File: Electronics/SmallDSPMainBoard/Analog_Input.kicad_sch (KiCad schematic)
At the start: 57 parts, among them J11 NC3FAAH2, J12 NC3FAAH2

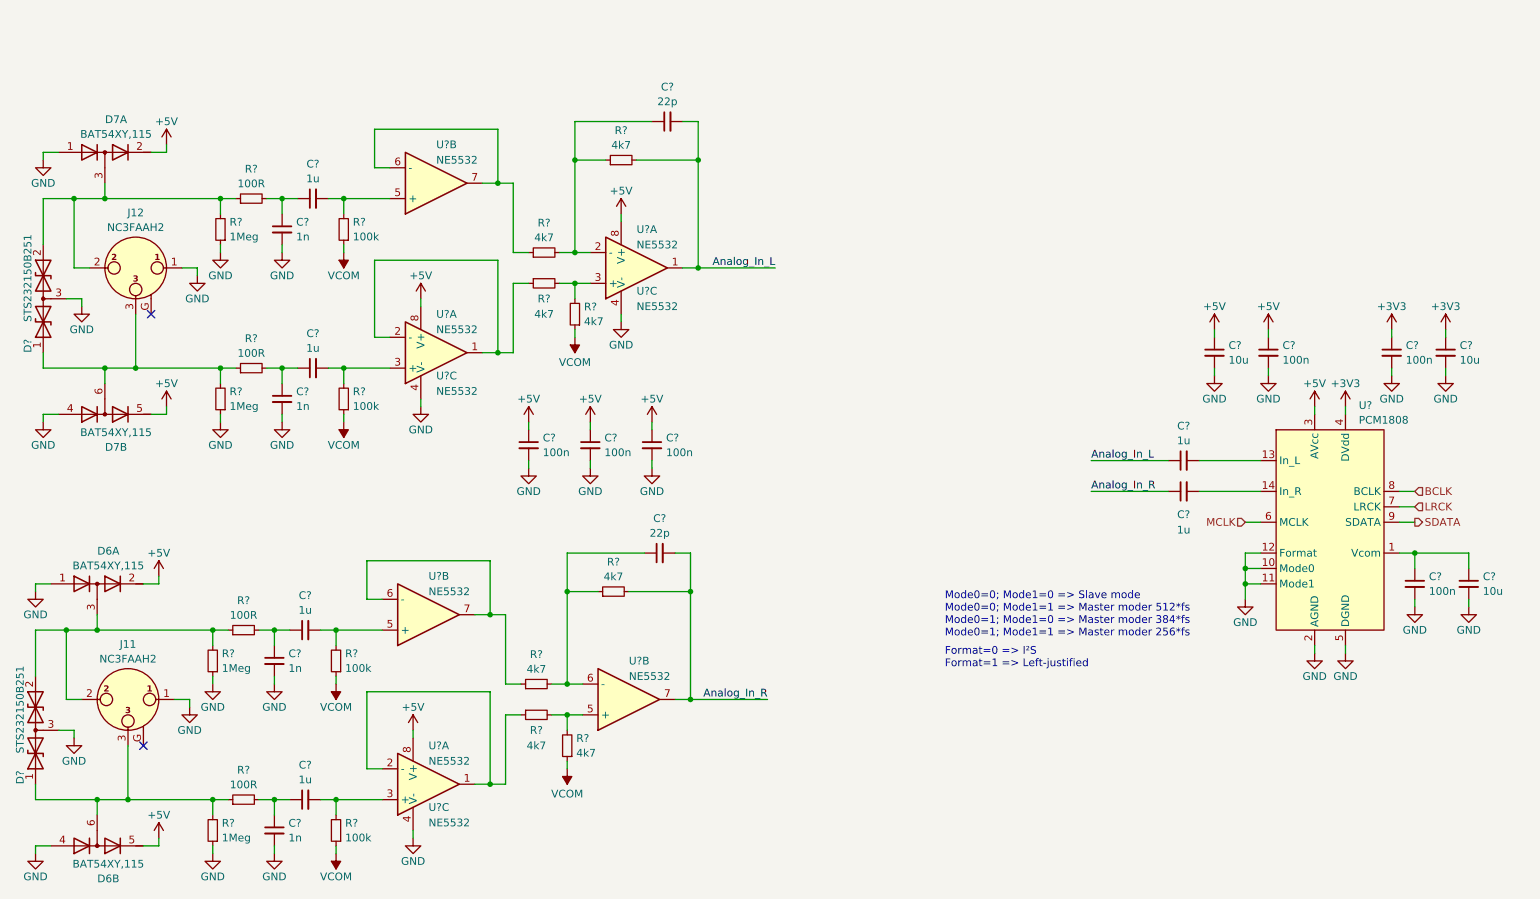
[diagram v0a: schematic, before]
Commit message: Partly finishes layout
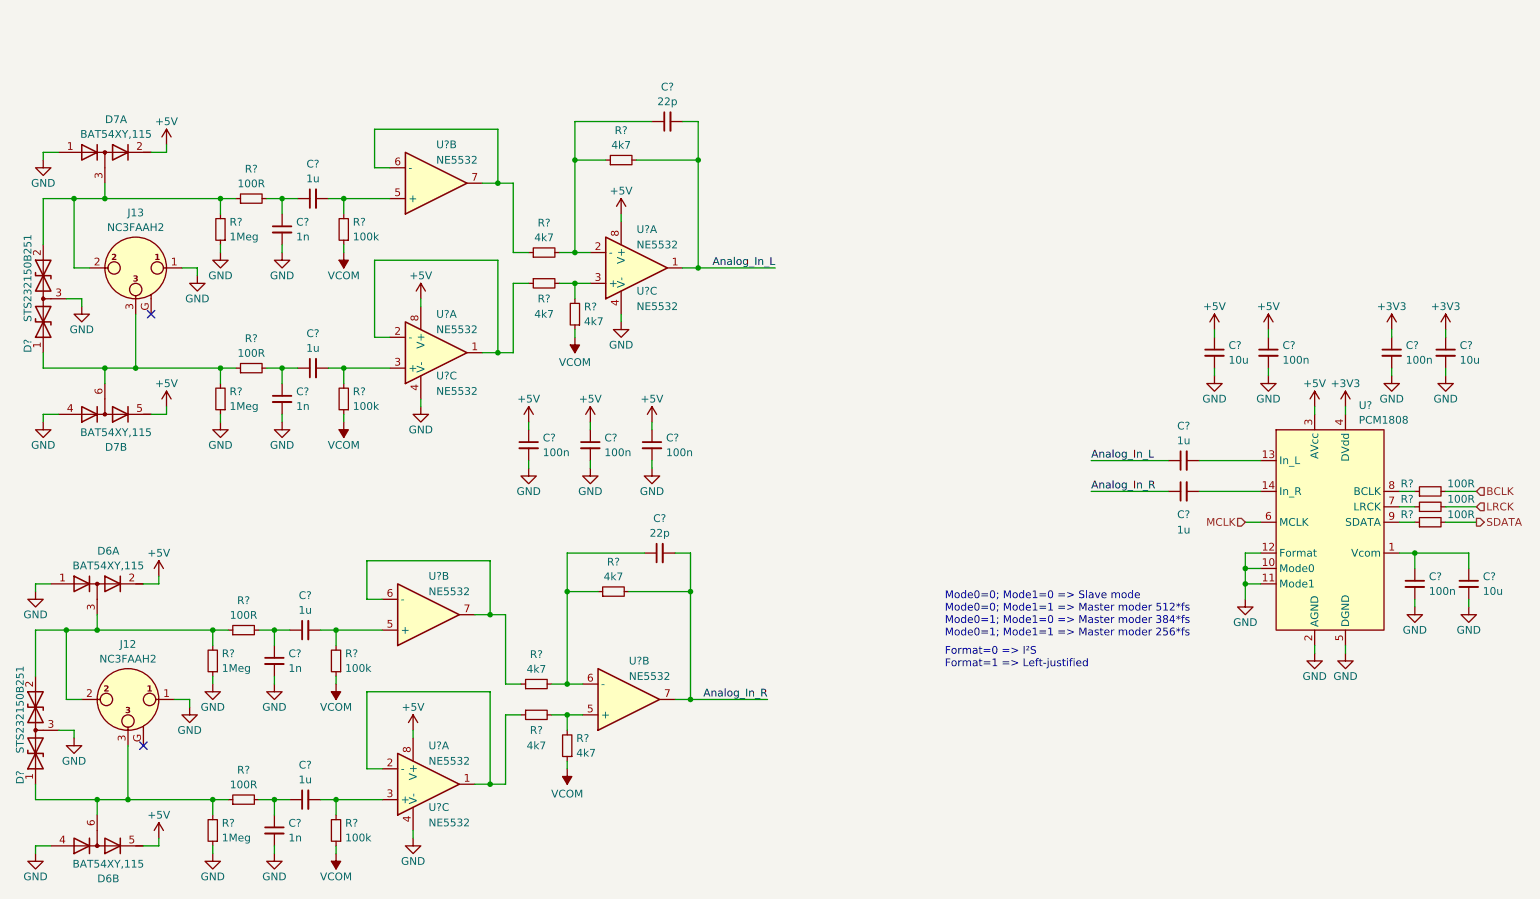
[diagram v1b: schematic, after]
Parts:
- added R? (x3): 100R, Resistor_SMD:R_0402_1005Metric, symbol Device:R_Small
- renumbered J11 to J12, J12 to J13
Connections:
- net BCLK: now also R?.2; no longer U?.8 (BCLK)
- net LRCK: now also R?.2; no longer U?.7 (LRCK)
- net SDATA: now also R?.2; no longer U?.9 (SDATA)
- new net: R?.1, U?.7 (LRCK)
- new net: R?.1, U?.8 (BCLK)
- new net: R?.1, U?.9 (SDATA)

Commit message: Finishes layout of Rev 1.0 and fixes a polarity error in the schematic
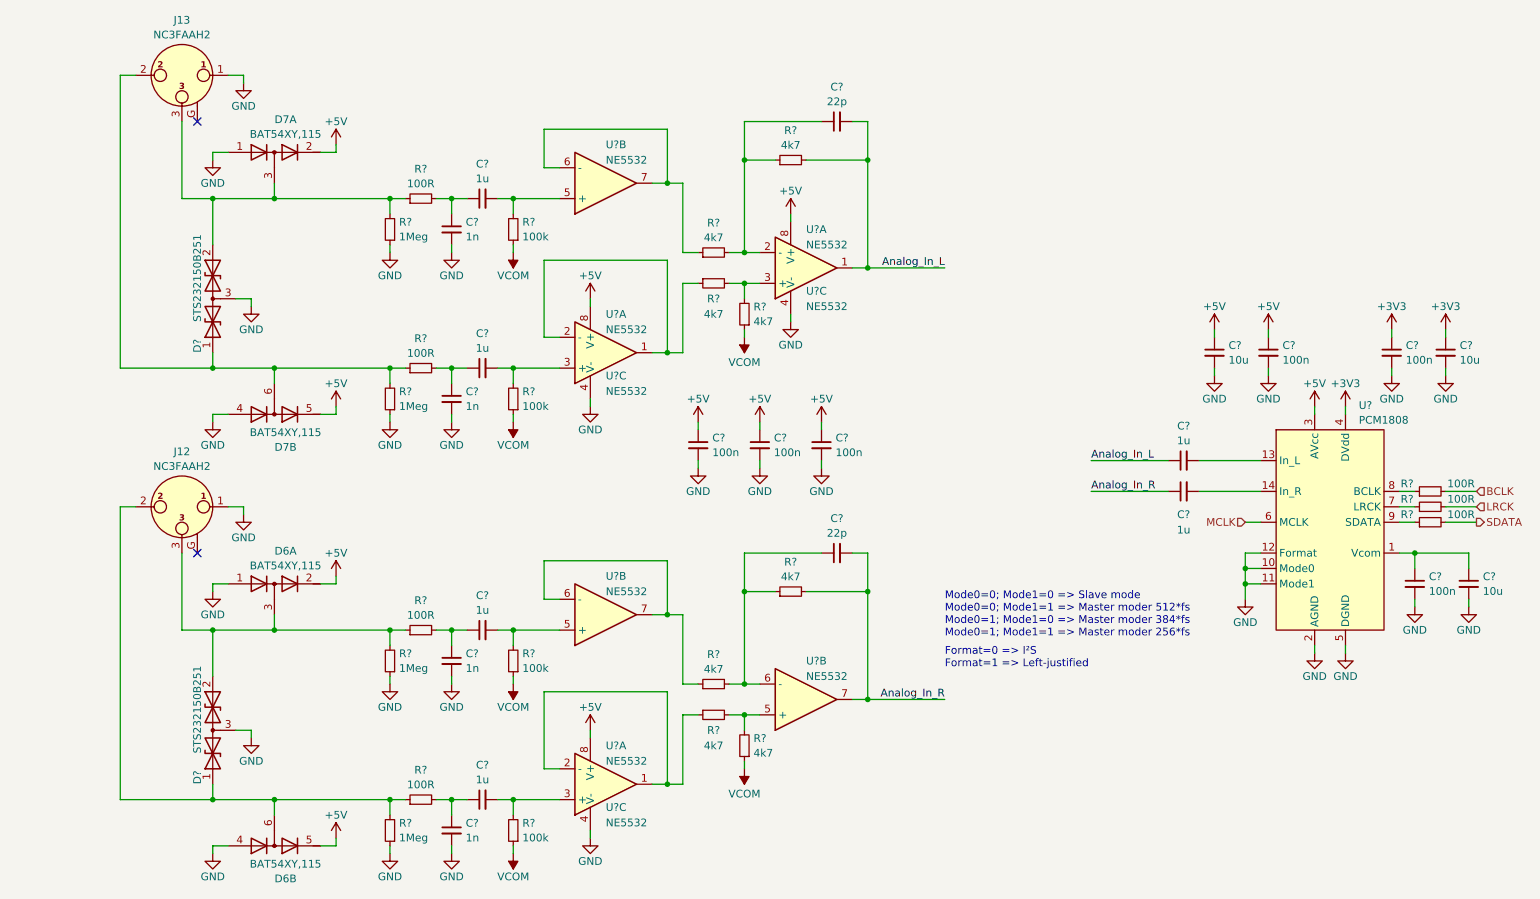
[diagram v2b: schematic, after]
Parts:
- U?: Part Number PCM1808 -> PCM1808PWR
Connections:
- net at D7.6 (C2), D?.1 (A1), R?.1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: now also J13.2; no longer J13.3
- net at D6.3 (C1), D?.2 (A2), R?.1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: now also J12.3; no longer J12.2
- net at D7.3 (C1), D?.2 (A2), R?.1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: now also J13.3; no longer J13.2
- net at D6.6 (C2), D?.1 (A1), R?.1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: now also J12.2; no longer J12.3
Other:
- moved on the sheet: C?, D6A, D6B, D7A, D7B, D?, J12, J13, R?, U?A, U?B, U?C
